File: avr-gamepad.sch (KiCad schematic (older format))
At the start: 33 parts, among them J1 Conn_01x08, J2 Conn_01x01, P1 USB_C_Plug_USB2.0, SW10 Up, SW11 Down, SW12 Left, SW13 Select, SW2 R, SW3 X, SW4 A, SW5 B, SW6 Start, SW7 Y, SW8 Right, SW9 L, U1 ATmega32U4-AU, Y1 16 MHz

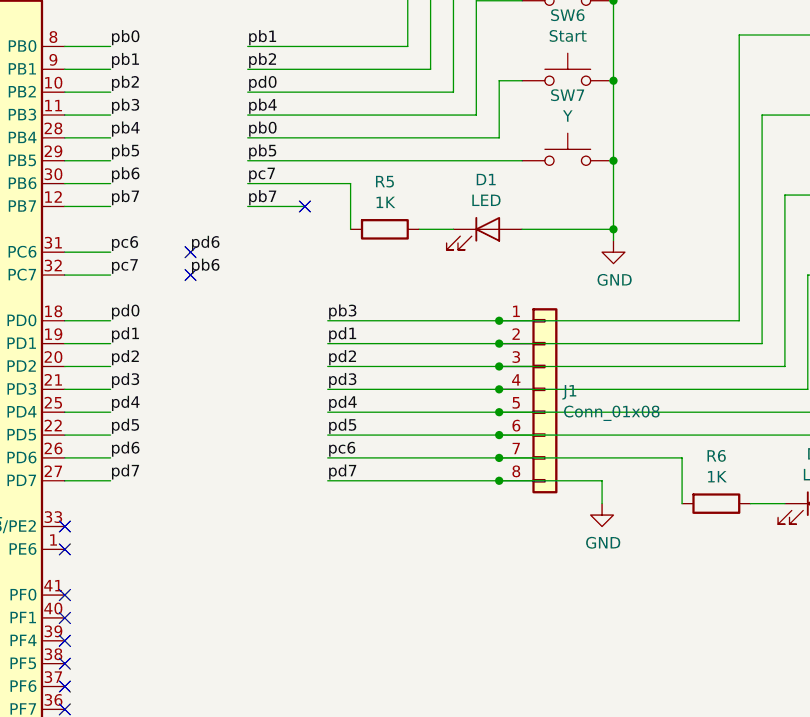
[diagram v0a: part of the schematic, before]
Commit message: replace headers with FFC connector. Adjust outline. Update gitignore
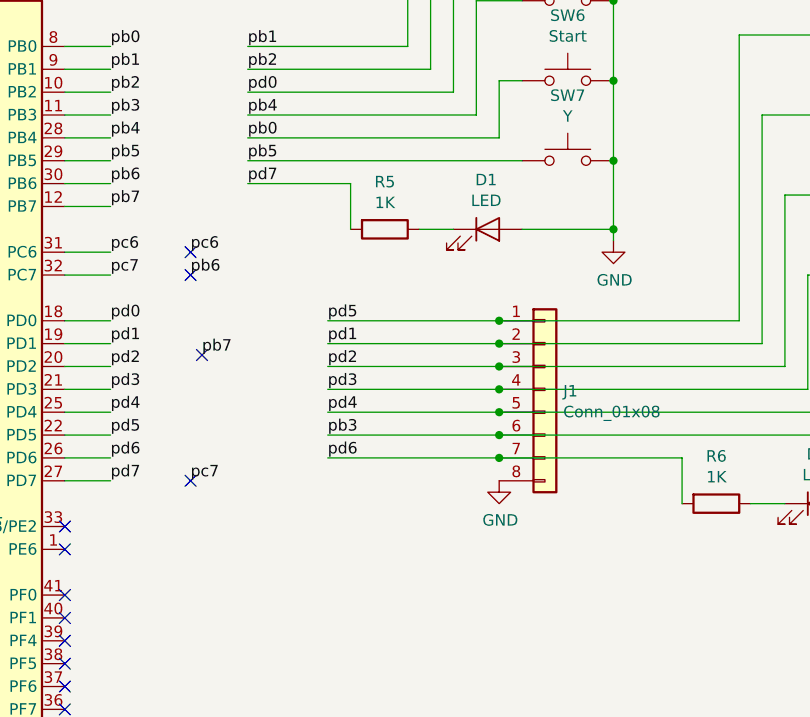
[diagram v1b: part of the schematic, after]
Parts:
- J1: footprint Connector_PinHeader_1.27mm:PinHeader_1x08_P1.27mm_Vertical -> Connector_FFC-FPC:Hirose_FH12-8S-0.5SH_1x08-1MP_P0.50mm_Horizontal
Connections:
- net GND: no longer U1.27 (PD7)
- net pb3: now also J1.6 (Pin_6), SW13.1; no longer J1.1 (Pin_1), SW9.1
- net pc6: no longer J1.7 (Pin_7), R6.2
- net pc7: no longer R5.2
- net pd5: now also J1.1 (Pin_1), SW9.1; no longer J1.6 (Pin_6), SW13.1
- net pd6: now also J1.7 (Pin_7), R6.2
- new net pd7: R5.2, U1.27 (PD7)
- no-connect marks 11 -> 12
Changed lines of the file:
@@
 	8050 2050 8550 2050
-$Comp
-L power:GND #PWR0116
-U 1 1 5CF1548A
-P 7450 4100
-F 0 "#PWR0116" H 7450 3850 50  0001 C CNN
-F 1 "GND" H 7455 3927 50  0000 C CNN
-F 2 "" H 7450 4100 50  0001 C CNN
-F 3 "" H 7450 4100 50  0001 C CNN
-	1    7450 4100
-	1    0    0    -1
-$EndComp
-Wire Wire Line
-	7450 4100 7450 4000
 $Comp
 L Device:LED D2
@@
 Wire Wire Line
 	1400 4400 1400 4550
-$Comp
-L Connector_Generic:Conn_01x08 J1
-U 1 1 5CF089CD
-P 7200 3600
-F 0 "J1" H 7280 3592 50  0000 L CNN
-F 1 "Conn_01x08" H 7280 3501 50  0000 L CNN
-F 2 "Connector_PinHeader_1.27mm:PinHeader_1x08_P1.27mm_Vertical" H 7200 3600 50  0001 C CNN
-F 3 "~" H 7200 3600 50  0001 C CNN
-	1    7200 3600
-	1    0    0    -1
-$EndComp
-Wire Wire Line
-	6250 4000 7000 4000
 Wire Wire Line
 	6250 3900 7000 3900
@@
 Wire Wire Line
 	7000 3900 7800 3900
-Connection ~ 7000 4000
-Wire Wire Line
-	7000 4000 7450 4000
 Text Label 5300 2800 0    50   ~ 0
 pb7
@@
 Wire Wire Line
 	5100 2800 5300 2800
-Text Label 5900 2500 0    50   ~ 0
-pb0
 Text Label 5900 2100 0    50   ~ 0
 pb1
 Text Label 5900 2200 0    50   ~ 0
 pb2
-Text Label 6250 3300 0    50   ~ 0
-pb3
 Text Label 5900 2400 0    50   ~ 0
 pb4
@@
 Text Label 6250 3700 0    50   ~ 0
 pd4
-Text Label 6250 3800 0    50   ~ 0
+Text Label 6250 3300 0    50   ~ 0
 pd5
-Text Label 6250 4000 0    50   ~ 0
+Text Label 5900 2700 0    50   ~ 0
 pd7
 Text Label 5300 3300 0    50   ~ 0
@@
 Wire Wire Line
 	5100 3900 5300 3900
-NoConn ~ 6150 2800
-Text Label 5900 2800 0    50   ~ 0
+NoConn ~ 5700 3450
+Text Label 5700 3450 0    50   ~ 0
 pb7
 NoConn ~ 5100 4300
-Wire Wire Line
-	6150 2800 5900 2800
 Text Label 5300 4000 0    50   ~ 0
 pd7
@@
 Wire Wire Line
 	5300 3000 5100 3000
-Text Label 6250 3900 0    50   ~ 0
+Text Label 5650 3000 0    50   ~ 0
 pc6
-Text Label 5900 2700 0    50   ~ 0
-pc7
 Text Label 5650 3100 0    50   ~ 0
 pb6
@@
 	1    0    0    -1
 $EndComp
-Text Label 5650 3000 0    50   ~ 0
+Text Label 6250 3900 0    50   ~ 0
 pd6
 NoConn ~ 5650 3000
+NoConn ~ 5650 4000
+$Comp
+L power:GND #PWR0113
+U 1 1 5D261ED2
+P 7000 4000
+F 0 "#PWR0113" H 7000 3750 50  0001 C CNN
+F 1 "GND" H 7005 3827 50  0000 C CNN
+F 2 "" H 7000 4000 50  0001 C CNN
+F 3 "" H 7000 4000 50  0001 C CNN
+	1    7000 4000
+	1    0    0    -1
+$EndComp
+$Comp
+L Connector_Generic:Conn_01x08 J1
+U 1 1 5CF089CD
+P 7200 3600
+F 0 "J1" H 7280 3592 50  0000 L CNN
+F 1 "Conn_01x08" H 7280 3501 50  0000 L CNN
+F 2 "Connector_FFC-FPC:Hirose_FH12-8S-0.5SH_1x08-1MP_P0.50mm_Horizontal" H 7200 3600 50  0001 C CNN
+F 3 "~" H 7200 3600 50  0001 C CNN
+	1    7200 3600
+	1    0    0    -1
+$EndComp
+Text Label 5650 4000 0    50   ~ 0
+pc7
+Text Label 6250 3800 0    50   ~ 0
+pb3
+Text Label 5900 2500 0    50   ~ 0
+pb0
 $EndSCHEMATC

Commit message: pin reassignments
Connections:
- net pb1: now also J1.6 (Pin_6), SW9.1; no longer SW2.1
- net pb3: now also SW2.1; no longer J1.6 (Pin_6), SW13.1
- net pd5: now also SW13.1; no longer SW9.1
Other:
- moved on the sheet: SW13, SW9
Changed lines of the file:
@@
 	8050 3300 8050 2050
-Wire Wire Line
-	8050 2050 8550 2050
-$Comp
-L Device:LED D2
-U 1 1 5CF1A9A2
-P 8400 4100
-F 0 "D2" H 8393 4316 50  0000 C CNN
-F 1 "LED" H 8393 4225 50  0000 C CNN
-F 2 "LED_SMD:LED_0805_2012Metric" H 8400 4100 50  0001 C CNN
-F 3 "~" H 8400 4100 50  0001 C CNN
-	1    8400 4100
-	1    0    0    -1
-$EndComp
-$Comp
-L Device:R R6
-U 1 1 5CF1BD3F
-P 7950 4100
-F 0 "R6" V 7743 4100 50  0000 C CNN
-F 1 "1K" V 7834 4100 50  0000 C CNN
-F 2 "Resistor_SMD:R_0805_2012Metric" V 7880 4100 50  0001 C CNN
-F 3 "~" H 7950 4100 50  0001 C CNN
-	1    7950 4100
-	0    1    1    0
-$EndComp
 Wire Wire Line
 	8950 3800 8950 4100
@@
 Wire Wire Line
 	8950 4100 8950 4150
-Wire Wire Line
-	8100 4100 8250 4100
 Wire Wire Line
 	7800 4100 7800 3900
@@
 Wire Wire Line
 	5100 2800 5300 2800
-Text Label 5900 2100 0    50   ~ 0
+Text Label 6250 3800 0    50   ~ 0
 pb1
 Text Label 5900 2200 0    50   ~ 0
@@
 $EndComp
 $Comp
-L Switch:SW_Push SW9
-U 1 1 5CF13385
-P 8750 2050
-F 0 "SW9" H 8750 2335 50  0000 C CNN
-F 1 "L" H 8750 2244 50  0000 C CNN
-F 2 "Button Contacts:Contact1" H 8750 2250 50  0001 C CNN
-F 3 "~" H 8750 2250 50  0001 C CNN
-	1    8750 2050
-	1    0    0    -1
-$EndComp
-$Comp
 L Switch:SW_Push SW3
 U 1 1 5CE36F95
@@
 $EndComp
 $Comp
-L Switch:SW_Push SW13
-U 1 1 5CF1336D
-P 8750 3800
-F 0 "SW13" H 8750 4085 50  0000 C CNN
-F 1 "Select" H 8750 3994 50  0000 C CNN
-F 2 "Button Contacts:Contact2" H 8750 4000 50  0001 C CNN
-F 3 "~" H 8750 4000 50  0001 C CNN
-	1    8750 3800
-	1    0    0    -1
-$EndComp
-$Comp
 L Switch:SW_Push SW2
 U 1 1 5CE355F4
@@
 Text Label 5650 4000 0    50   ~ 0
 pc7
-Text Label 6250 3800 0    50   ~ 0
+Text Label 5900 2100 0    50   ~ 0
 pb3
 Text Label 5900 2500 0    50   ~ 0
 pb0
+Wire Wire Line
+	8050 2050 8550 2050
+$Comp
+L Switch:SW_Push SW9
+U 1 1 5CF13385
+P 8750 3800
+F 0 "SW9" H 8750 4085 50  0000 C CNN
+F 1 "L" H 8750 3994 50  0000 C CNN
+F 2 "Button Contacts:Contact1" H 8750 4000 50  0001 C CNN
+F 3 "~" H 8750 4000 50  0001 C CNN
+	1    8750 3800
+	1    0    0    -1
+$EndComp
+Wire Wire Line
+	8100 4100 8250 4100
+$Comp
+L Device:R R6
+U 1 1 5CF1BD3F
+P 7950 4100
+F 0 "R6" V 7743 4100 50  0000 C CNN
+F 1 "1K" V 7834 4100 50  0000 C CNN
+F 2 "Resistor_SMD:R_0805_2012Metric" V 7880 4100 50  0001 C CNN
+F 3 "~" H 7950 4100 50  0001 C CNN
+	1    7950 4100
+	0    1    1    0
+$EndComp
+$Comp
+L Device:LED D2
+U 1 1 5CF1A9A2
+P 8400 4100
+F 0 "D2" H 8393 4316 50  0000 C CNN
+F 1 "LED" H 8393 4225 50  0000 C CNN
+F 2 "LED_SMD:LED_0805_2012Metric" H 8400 4100 50  0001 C CNN
+F 3 "~" H 8400 4100 50  0001 C CNN
+	1    8400 4100
+	1    0    0    -1
+$EndComp
+$Comp
+L Switch:SW_Push SW13
+U 1 1 5CF1336D
+P 8750 2050
+F 0 "SW13" H 8750 2335 50  0000 C CNN
+F 1 "Select" H 8750 2244 50  0000 C CNN
+F 2 "Button Contacts:Contact2" H 8750 2250 50  0001 C CNN
+F 3 "~" H 8750 2250 50  0001 C CNN
+	1    8750 2050
+	1    0    0    -1
+$EndComp
 $EndSCHEMATC

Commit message: move FFC back, improve routing
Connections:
- net pb7: now also J1.3 (Pin_3), SW10.1
- net pc6: now also SW4.1
- net pd0: no longer SW4.1
- net pd2: no longer J1.3 (Pin_3), SW10.1
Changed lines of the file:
@@
 Text Label 5900 2600 0    50   ~ 0
 pb5
-Text Label 5900 2300 0    50   ~ 0
-pd0
 Text Label 6250 3400 0    50   ~ 0
 pd1
-Text Label 6250 3500 0    50   ~ 0
+Text Label 5700 3450 0    50   ~ 0
 pd2
 Text Label 6250 3600 0    50   ~ 0
@@
 	5100 3900 5300 3900
 NoConn ~ 5700 3450
-Text Label 5700 3450 0    50   ~ 0
+Text Label 6250 3500 0    50   ~ 0
 pb7
 NoConn ~ 5100 4300
@@
 Wire Wire Line
 	5300 3000 5100 3000
-Text Label 5650 3000 0    50   ~ 0
+Text Label 5900 2300 0    50   ~ 0
 pc6
 Text Label 5650 3100 0    50   ~ 0
@@
 Text Label 5650 4000 0    50   ~ 0
 pc7
-Text Label 5900 2100 0    50   ~ 0
-pb3
 Text Label 5900 2500 0    50   ~ 0
 pb0
@@
 	1    0    0    -1
 $EndComp
+Text Label 5900 2100 0    50   ~ 0
+pb3
+Text Label 5650 3000 0    50   ~ 0
+pd0
 $EndSCHEMATC

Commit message: begin v2. Remove flex, move components to one side, expand board size, remove excess caps, recess usb connector
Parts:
- removed C2, C3: 0.1uF, Capacitor_SMD:C_0805_2012Metric, symbol Device:CP1
- removed J2: Conn_01x01, Connector_PinHeader_1.27mm:PinHeader_1x01_P1.27mm_Vertical, symbol Connector_Generic:Conn_01x01
- added SW1: RESET, Button Contacts:Small, symbol Switch:SW_Push
- C1, C4, C5, C6, C7, C8: symbol Device:CP1 -> Device:C
- SW10, SW11, SW12, SW2, SW3, SW4, SW5, SW7, SW8, SW9: footprint Button Contacts:Contact1 -> Button Contacts:Large_tapered
- SW13, SW6: footprint Button Contacts:Contact2 -> Button Contacts:Small
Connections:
- net GND: now also SW1.1
- net at U1.13 (~RESET): now also SW1.2
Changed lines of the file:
@@
 	3150 2550 3150 2400
 Connection ~ 3150 2400
-Text Notes 3500 2200 0    50   ~ 0
+Text Notes 3400 2200 0    50   ~ 0
 Freq crystal
 Wire Wire Line
@@
 	4500 1650 4600 1650
 $Comp
-L Device:CP1 C1
+L Device:C C1
 U 1 1 5CE336BE
 P 1150 1700
@@
 Connection ~ 1150 1850
 $Comp
-L Device:CP1 C4
+L Device:C C4
 U 1 1 5CE34260
 P 2350 1700
@@
 $EndComp
 Connection ~ 2350 1550
-Wire Wire Line
-	1150 1550 1600 1550
-Wire Wire Line
-	1150 1850 1600 1850
-$Comp
-L Device:CP1 C2
-U 1 1 5CE35BE6
-P 1600 1700
-F 0 "C2" H 1715 1746 50  0000 L CNN
-F 1 "0.1uF" H 1715 1655 50  0000 L CNN
-F 2 "Capacitor_SMD:C_0805_2012Metric" H 1600 1700 50  0001 C CNN
-F 3 "~" H 1600 1700 50  0001 C CNN
-	1    1600 1700
-	1    0    0    -1
-$EndComp
-Connection ~ 1600 1550
-Connection ~ 1600 1850
-Wire Wire Line
-	1600 1550 2000 1550
-Wire Wire Line
-	1600 1850 2000 1850
-Connection ~ 2000 1550
-Wire Wire Line
-	2000 1550 2350 1550
-Connection ~ 2000 1850
-Wire Wire Line
-	2000 1850 2350 1850
-$Comp
-L Device:CP1 C5
+$Comp
+L Device:C C5
 U 1 1 5CE36ECF
 P 3300 2250
@@
 $EndComp
 $Comp
-L Device:CP1 C6
+L Device:C C6
 U 1 1 5CE373C9
 P 3300 2550
@@
 	3850 3400 3900 3400
 $Comp
-L Device:CP1 C8
+L Device:C C8
 U 1 1 5CE37ACD
 P 3700 4100
@@
 F 3 "~" H 3700 4100 50  0001 C CNN
 	1    3700 4100
-	1    0    0    -1
-$EndComp
-$Comp
-L Device:CP1 C3
-U 1 1 5CE36419
-P 2000 1700
-F 0 "C3" H 2115 1746 50  0000 L CNN
-F 1 "0.1uF" H 2115 1655 50  0000 L CNN
-F 2 "Capacitor_SMD:C_0805_2012Metric" H 2000 1700 50  0001 C CNN
-F 3 "~" H 2000 1700 50  0001 C CNN
-	1    2000 1700
 	1    0    0    -1
 $EndComp
@@
 	3650 3650 3300 3650
 $Comp
-L Device:CP1 C7
+L Device:C C7
 U 1 1 5CE3DF92
 P 3300 4100
@@
 Wire Wire Line
 	2200 4250 2350 4250
-Wire Wire Line
-	3850 2100 3850 2000
-Wire Wire Line
-	3850 2000 3800 2000
-$Comp
-L Connector_Generic:Conn_01x01 J2
-U 1 1 5CF75073
-P 3600 2000
-F 0 "J2" H 3518 1775 50  0000 C CNN
-F 1 "Conn_01x01" H 3518 1866 50  0000 C CNN
-F 2 "Connector_PinHeader_1.27mm:PinHeader_1x01_P1.27mm_Vertical" H 3600 2000 50  0001 C CNN
-F 3 "~" H 3600 2000 50  0001 C CNN
-	1    3600 2000
-	-1   0    0    1
-$EndComp
 Wire Wire Line
 	1400 4400 1400 4550
@@
 F 0 "SW8" H 8750 2685 50  0000 C CNN
 F 1 "Right" H 8750 2594 50  0000 C CNN
-F 2 "Button Contacts:Contact1" H 8750 2600 50  0001 C CNN
+F 2 "Button Contacts:Large_tapered" H 8750 2600 50  0001 C CNN
 F 3 "~" H 8750 2600 50  0001 C CNN
 	1    8750 2400
@@
 F 0 "SW12" H 8750 3735 50  0000 C CNN
 F 1 "Left" H 8750 3644 50  0000 C CNN
-F 2 "Button Contacts:Contact1" H 8750 3650 50  0001 C CNN
+F 2 "Button Contacts:Large_tapered" H 8750 3650 50  0001 C CNN
 F 3 "~" H 8750 3650 50  0001 C CNN
 	1    8750 3450
@@
 F 0 "SW10" H 8750 3035 50  0000 C CNN
 F 1 "Up" H 8750 2944 50  0000 C CNN
-F 2 "Button Contacts:Contact1" H 8750 2950 50  0001 C CNN
+F 2 "Button Contacts:Large_tapered" H 8750 2950 50  0001 C CNN
 F 3 "~" H 8750 2950 50  0001 C CNN
 	1    8750 2750
@@
 F 0 "SW3" H 7300 1485 50  0000 C CNN
 F 1 "X" H 7300 1394 50  0000 C CNN
-F 2 "Button Contacts:Contact1" H 7300 1400 50  0001 C CNN
+F 2 "Button Contacts:Large_tapered" H 7300 1400 50  0001 C CNN
 F 3 "~" H 7300 1400 50  0001 C CNN
 	1    7300 1200
@@
 F 0 "SW7" H 7300 2885 50  0000 C CNN
 F 1 "Y" H 7300 2794 50  0000 C CNN
-F 2 "Button Contacts:Contact1" H 7300 2800 50  0001 C CNN
+F 2 "Button Contacts:Large_tapered" H 7300 2800 50  0001 C CNN
 F 3 "~" H 7300 2800 50  0001 C CNN
 	1    7300 2600
@@
 F 0 "SW4" H 7300 1835 50  0000 C CNN
 F 1 "A" H 7300 1744 50  0000 C CNN
-F 2 "Button Contacts:Contact1" H 7300 1750 50  0001 C CNN
+F 2 "Button Contacts:Large_tapered" H 7300 1750 50  0001 C CNN
 F 3 "~" H 7300 1750 50  0001 C CNN
 	1    7300 1550
@@
 F 0 "SW5" H 7300 2185 50  0000 C CNN
 F 1 "B" H 7300 2094 50  0000 C CNN
-F 2 "Button Contacts:Contact1" H 7300 2100 50  0001 C CNN
+F 2 "Button Contacts:Large_tapered" H 7300 2100 50  0001 C CNN
 F 3 "~" H 7300 2100 50  0001 C CNN
 	1    7300 1900
@@
 F 0 "SW2" H 7300 1135 50  0000 C CNN
 F 1 "R" H 7300 1044 50  0000 C CNN
-F 2 "Button Contacts:Contact1" H 7300 1050 50  0001 C CNN
+F 2 "Button Contacts:Large_tapered" H 7300 1050 50  0001 C CNN
 F 3 "~" H 7300 1050 50  0001 C CNN
 	1    7300 850
@@
 F 0 "SW6" H 7300 2535 50  0000 C CNN
 F 1 "Start" H 7300 2444 50  0000 C CNN
-F 2 "Button Contacts:Contact2" H 7300 2450 50  0001 C CNN
+F 2 "Button Contacts:Small" H 7300 2450 50  0001 C CNN
 F 3 "~" H 7300 2450 50  0001 C CNN
 	1    7300 2250
@@
 F 0 "SW11" H 8750 3385 50  0000 C CNN
 F 1 "Down" H 8750 3294 50  0000 C CNN
-F 2 "Button Contacts:Contact1" H 8750 3300 50  0001 C CNN
+F 2 "Button Contacts:Large_tapered" H 8750 3300 50  0001 C CNN
 F 3 "~" H 8750 3300 50  0001 C CNN
 	1    8750 3100
@@
 F 0 "SW9" H 8750 4085 50  0000 C CNN
 F 1 "L" H 8750 3994 50  0000 C CNN
-F 2 "Button Contacts:Contact1" H 8750 4000 50  0001 C CNN
+F 2 "Button Contacts:Large_tapered" H 8750 4000 50  0001 C CNN
 F 3 "~" H 8750 4000 50  0001 C CNN
 	1    8750 3800
@@
 F 0 "SW13" H 8750 2335 50  0000 C CNN
 F 1 "Select" H 8750 2244 50  0000 C CNN
-F 2 "Button Contacts:Contact2" H 8750 2250 50  0001 C CNN
+F 2 "Button Contacts:Small" H 8750 2250 50  0001 C CNN
 F 3 "~" H 8750 2250 50  0001 C CNN
 	1    8750 2050
@@
 Text Label 5650 3000 0    50   ~ 0
 pd0
+$Comp
+L Switch:SW_Push SW1
+U 1 1 5D8F3544
+P 3600 1800
+F 0 "SW1" H 3600 2085 50  0000 C CNN
+F 1 "RESET" H 3600 1994 50  0000 C CNN
+F 2 "Button Contacts:Small" H 3600 2000 50  0001 C CNN
+F 3 "~" H 3600 2000 50  0001 C CNN
+	1    3600 1800
+	1    0    0    -1
+$EndComp
+Wire Wire Line
+	3850 2100 3850 1800
+Wire Wire Line
+	3850 1800 3800 1800
+$Comp
+L power:GND #PWR02
+U 1 1 5D8FA225
+P 3100 1800
+F 0 "#PWR02" H 3100 1550 50  0001 C CNN
+F 1 "GND" H 3105 1627 50  0000 C CNN
+F 2 "" H 3100 1800 50  0001 C CNN
+F 3 "" H 3100 1800 50  0001 C CNN
+	1    3100 1800
+	1    0    0    -1
+$EndComp
+Wire Wire Line
+	3100 1800 3400 1800
+Wire Wire Line
+	1150 1550 2350 1550
+Wire Wire Line
+	1150 1850 2350 1850
 $EndSCHEMATC

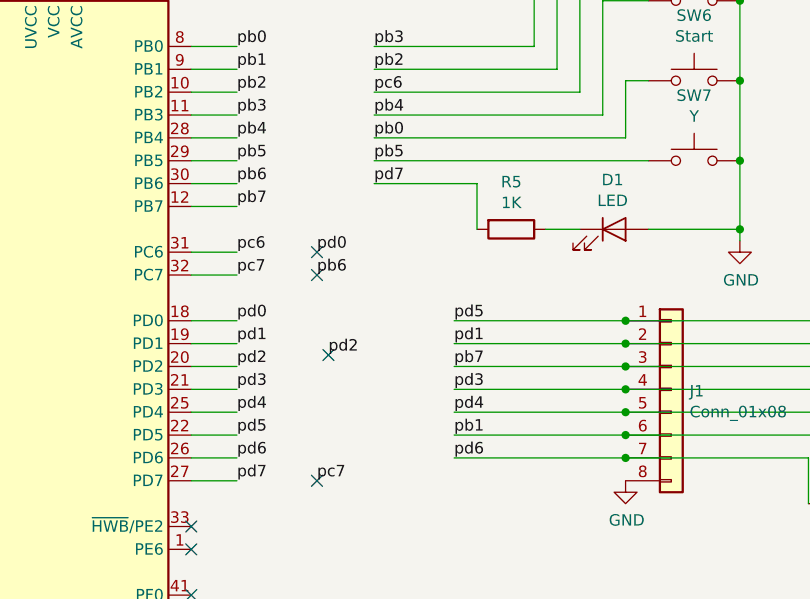
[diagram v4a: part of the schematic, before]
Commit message: pin swapping and component shuffling
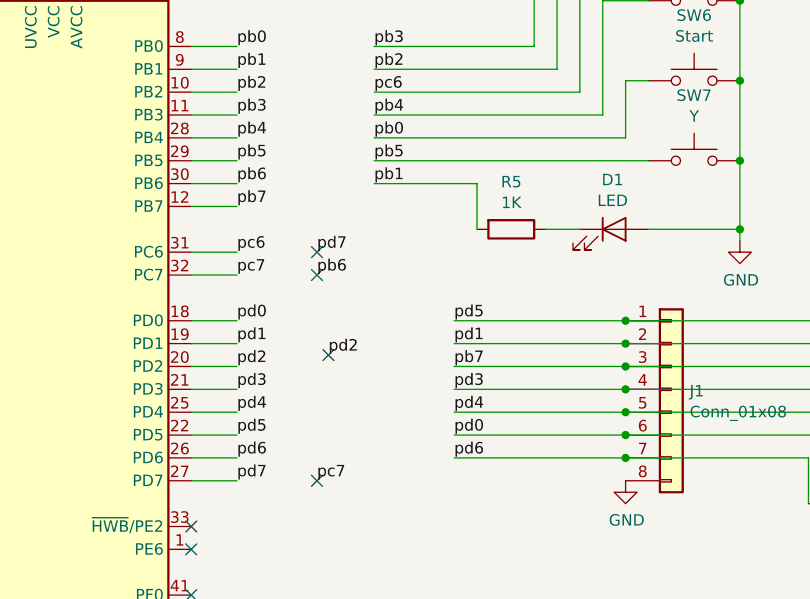
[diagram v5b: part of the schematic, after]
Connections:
- net pb1: now also R5.2; no longer J1.6 (Pin_6), SW9.1
- net pd0: now also J1.6 (Pin_6), SW9.1
- net pd7: no longer R5.2
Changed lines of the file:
@@
 Wire Wire Line
 	5100 2800 5300 2800
-Text Label 6250 3800 0    50   ~ 0
+Text Label 5900 2700 0    50   ~ 0
 pb1
 Text Label 5900 2200 0    50   ~ 0
@@
 Text Label 6250 3300 0    50   ~ 0
 pd5
-Text Label 5900 2700 0    50   ~ 0
+Text Label 5650 3000 0    50   ~ 0
 pd7
 Text Label 5300 3300 0    50   ~ 0
@@
 Text Label 5900 2100 0    50   ~ 0
 pb3
-Text Label 5650 3000 0    50   ~ 0
+Text Label 6250 3800 0    50   ~ 0
 pd0
 $Comp

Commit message: move footprints to new dir, increase contact size, add squidward
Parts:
- SW1, SW13, SW6: footprint Button Contacts:Small -> button-contacts:Small
- SW10, SW11, SW12, SW2, SW3, SW4, SW5, SW7, SW8, SW9: footprint Button Contacts:Large_tapered -> button-contacts:Large_tapered
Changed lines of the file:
@@
 F 0 "SW8" H 8750 2685 50  0000 C CNN
 F 1 "Right" H 8750 2594 50  0000 C CNN
-F 2 "Button Contacts:Large_tapered" H 8750 2600 50  0001 C CNN
+F 2 "button-contacts:Large_tapered" H 8750 2600 50  0001 C CNN
 F 3 "~" H 8750 2600 50  0001 C CNN
 	1    8750 2400
@@
 F 0 "SW12" H 8750 3735 50  0000 C CNN
 F 1 "Left" H 8750 3644 50  0000 C CNN
-F 2 "Button Contacts:Large_tapered" H 8750 3650 50  0001 C CNN
+F 2 "button-contacts:Large_tapered" H 8750 3650 50  0001 C CNN
 F 3 "~" H 8750 3650 50  0001 C CNN
 	1    8750 3450
@@
 F 0 "SW10" H 8750 3035 50  0000 C CNN
 F 1 "Up" H 8750 2944 50  0000 C CNN
-F 2 "Button Contacts:Large_tapered" H 8750 2950 50  0001 C CNN
+F 2 "button-contacts:Large_tapered" H 8750 2950 50  0001 C CNN
 F 3 "~" H 8750 2950 50  0001 C CNN
 	1    8750 2750
@@
 F 0 "SW3" H 7300 1485 50  0000 C CNN
 F 1 "X" H 7300 1394 50  0000 C CNN
-F 2 "Button Contacts:Large_tapered" H 7300 1400 50  0001 C CNN
+F 2 "button-contacts:Large_tapered" H 7300 1400 50  0001 C CNN
 F 3 "~" H 7300 1400 50  0001 C CNN
 	1    7300 1200
@@
 F 0 "SW7" H 7300 2885 50  0000 C CNN
 F 1 "Y" H 7300 2794 50  0000 C CNN
-F 2 "Button Contacts:Large_tapered" H 7300 2800 50  0001 C CNN
+F 2 "button-contacts:Large_tapered" H 7300 2800 50  0001 C CNN
 F 3 "~" H 7300 2800 50  0001 C CNN
 	1    7300 2600
@@
 F 0 "SW4" H 7300 1835 50  0000 C CNN
 F 1 "A" H 7300 1744 50  0000 C CNN
-F 2 "Button Contacts:Large_tapered" H 7300 1750 50  0001 C CNN
+F 2 "button-contacts:Large_tapered" H 7300 1750 50  0001 C CNN
 F 3 "~" H 7300 1750 50  0001 C CNN
 	1    7300 1550
@@
 F 0 "SW5" H 7300 2185 50  0000 C CNN
 F 1 "B" H 7300 2094 50  0000 C CNN
-F 2 "Button Contacts:Large_tapered" H 7300 2100 50  0001 C CNN
+F 2 "button-contacts:Large_tapered" H 7300 2100 50  0001 C CNN
 F 3 "~" H 7300 2100 50  0001 C CNN
 	1    7300 1900
@@
 F 0 "SW2" H 7300 1135 50  0000 C CNN
 F 1 "R" H 7300 1044 50  0000 C CNN
-F 2 "Button Contacts:Large_tapered" H 7300 1050 50  0001 C CNN
+F 2 "button-contacts:Large_tapered" H 7300 1050 50  0001 C CNN
 F 3 "~" H 7300 1050 50  0001 C CNN
 	1    7300 850
@@
 F 0 "SW6" H 7300 2535 50  0000 C CNN
 F 1 "Start" H 7300 2444 50  0000 C CNN
-F 2 "Button Contacts:Small" H 7300 2450 50  0001 C CNN
+F 2 "button-contacts:Small" H 7300 2450 50  0001 C CNN
 F 3 "~" H 7300 2450 50  0001 C CNN
 	1    7300 2250
@@
 F 0 "SW11" H 8750 3385 50  0000 C CNN
 F 1 "Down" H 8750 3294 50  0000 C CNN
-F 2 "Button Contacts:Large_tapered" H 8750 3300 50  0001 C CNN
+F 2 "button-contacts:Large_tapered" H 8750 3300 50  0001 C CNN
 F 3 "~" H 8750 3300 50  0001 C CNN
 	1    8750 3100
@@
 F 0 "SW9" H 8750 4085 50  0000 C CNN
 F 1 "L" H 8750 3994 50  0000 C CNN
-F 2 "Button Contacts:Large_tapered" H 8750 4000 50  0001 C CNN
+F 2 "button-contacts:Large_tapered" H 8750 4000 50  0001 C CNN
 F 3 "~" H 8750 4000 50  0001 C CNN
 	1    8750 3800
@@
 F 0 "SW13" H 8750 2335 50  0000 C CNN
 F 1 "Select" H 8750 2244 50  0000 C CNN
-F 2 "Button Contacts:Small" H 8750 2250 50  0001 C CNN
+F 2 "button-contacts:Small" H 8750 2250 50  0001 C CNN
 F 3 "~" H 8750 2250 50  0001 C CNN
 	1    8750 2050
@@
 F 0 "SW1" H 3600 2085 50  0000 C CNN
 F 1 "RESET" H 3600 1994 50  0000 C CNN
-F 2 "Button Contacts:Small" H 3600 2000 50  0001 C CNN
+F 2 "button-contacts:Small" H 3600 2000 50  0001 C CNN
 F 3 "~" H 3600 2000 50  0001 C CNN
 	1    3600 1800
